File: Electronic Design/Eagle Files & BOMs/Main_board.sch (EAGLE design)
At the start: 35 parts, among them IC1 ACS712ELC-5A, IC2 ATMEGA328-PU, Q1 IRF9540, Q2 IRF9540, X1 16MHz

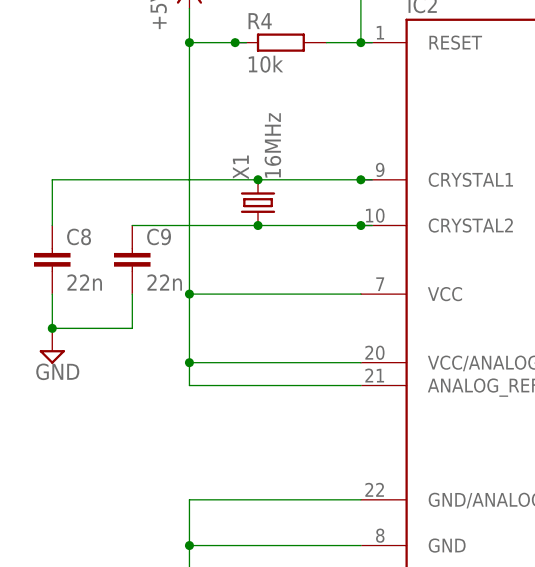
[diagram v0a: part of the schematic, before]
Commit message: correcting cap values on atmega crystal
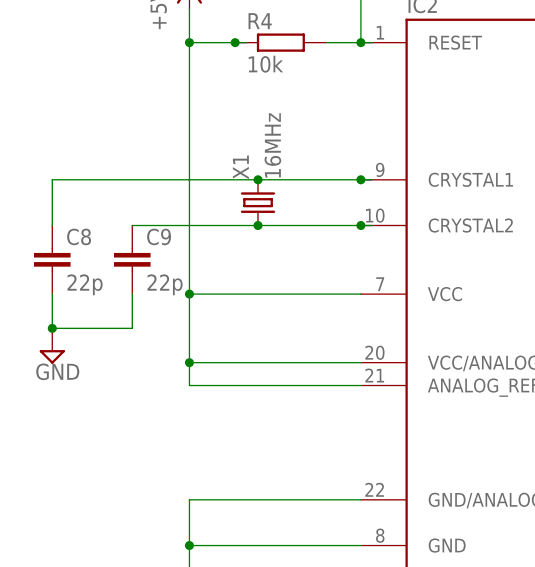
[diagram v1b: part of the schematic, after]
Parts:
- C8, C9: value 22n -> 22p
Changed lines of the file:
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@@
 <part name="+5V1" library="supply1" deviceset="+5V" device=""/>
 <part name="C7" library="resistor" deviceset="C-EU" device="C1206K" value="0.1u"/>
-<part name="C9" library="resistor" deviceset="C-EU" device="C0805K" value="22n"/>
-<part name="C8" library="resistor" deviceset="C-EU" device="C0805K" value="22n"/>
+<part name="C9" library="resistor" deviceset="C-EU" device="C0805K" value="22p"/>
+<part name="C8" library="resistor" deviceset="C-EU" device="C0805K" value="22p"/>
 <part name="SUPPLY14" library="supply2" deviceset="GND" device=""/>
 <part name="SUPPLY17" library="supply2" deviceset="GND" device=""/>

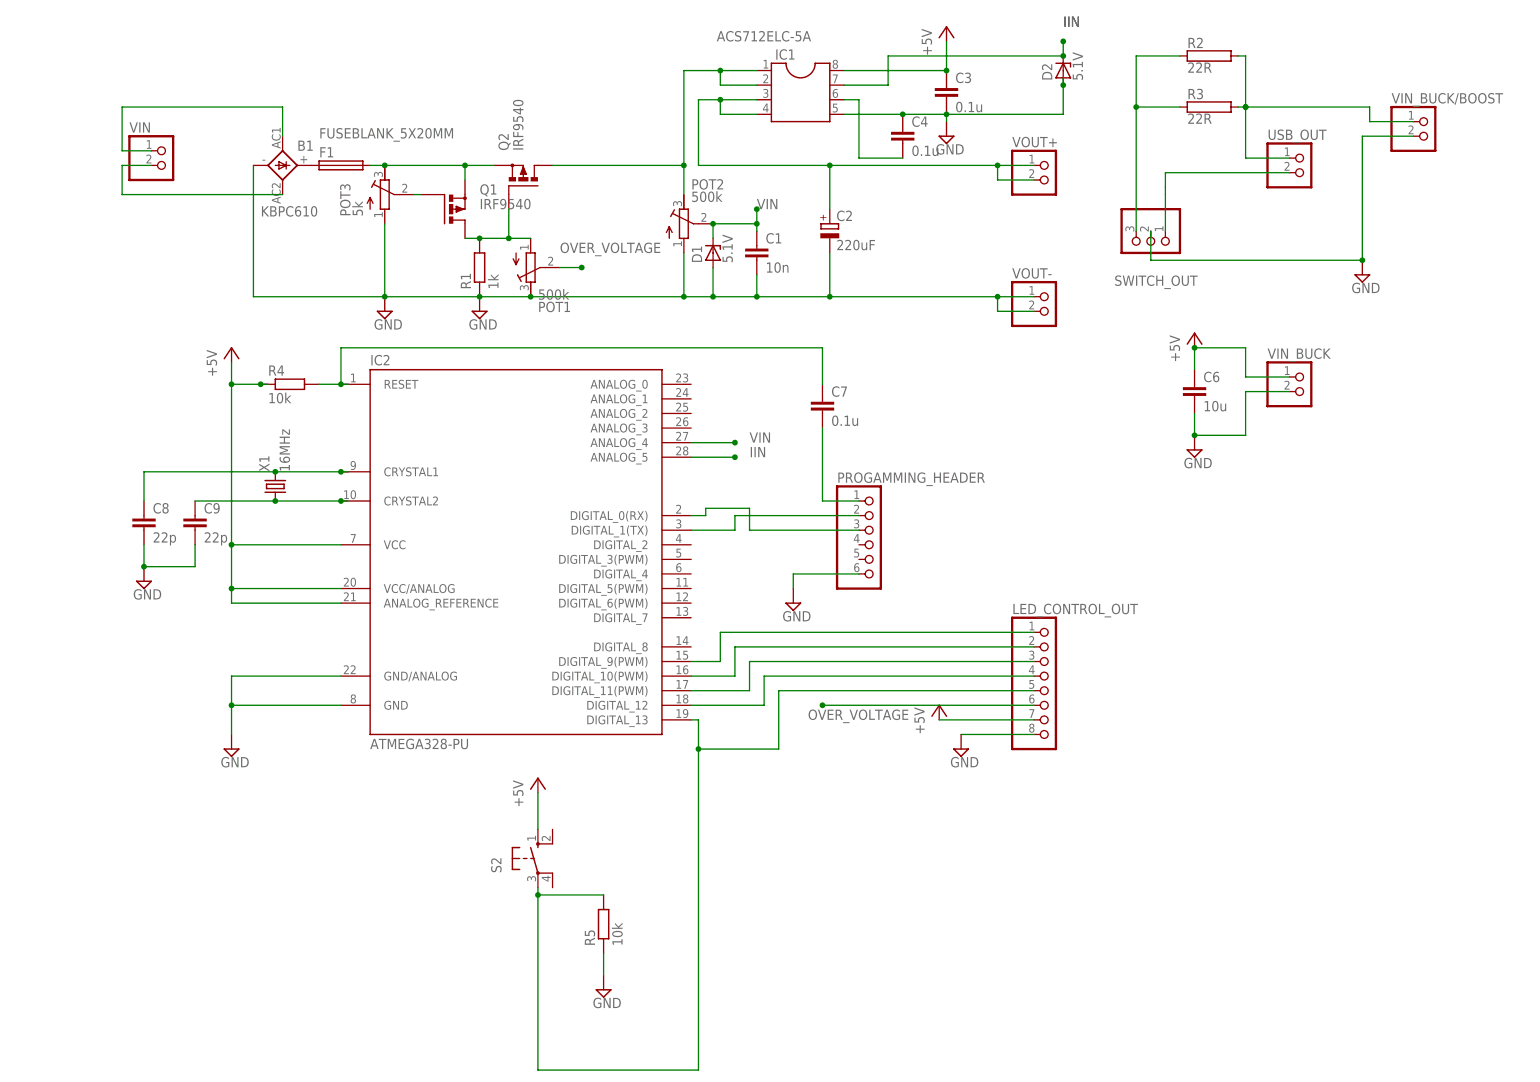
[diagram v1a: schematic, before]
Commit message: added overvoltage protection, replaced fuse holder footprint, stopped irfs from overlapping with ground stitching vias, moved dummy load resistors and corrected pin header pitch
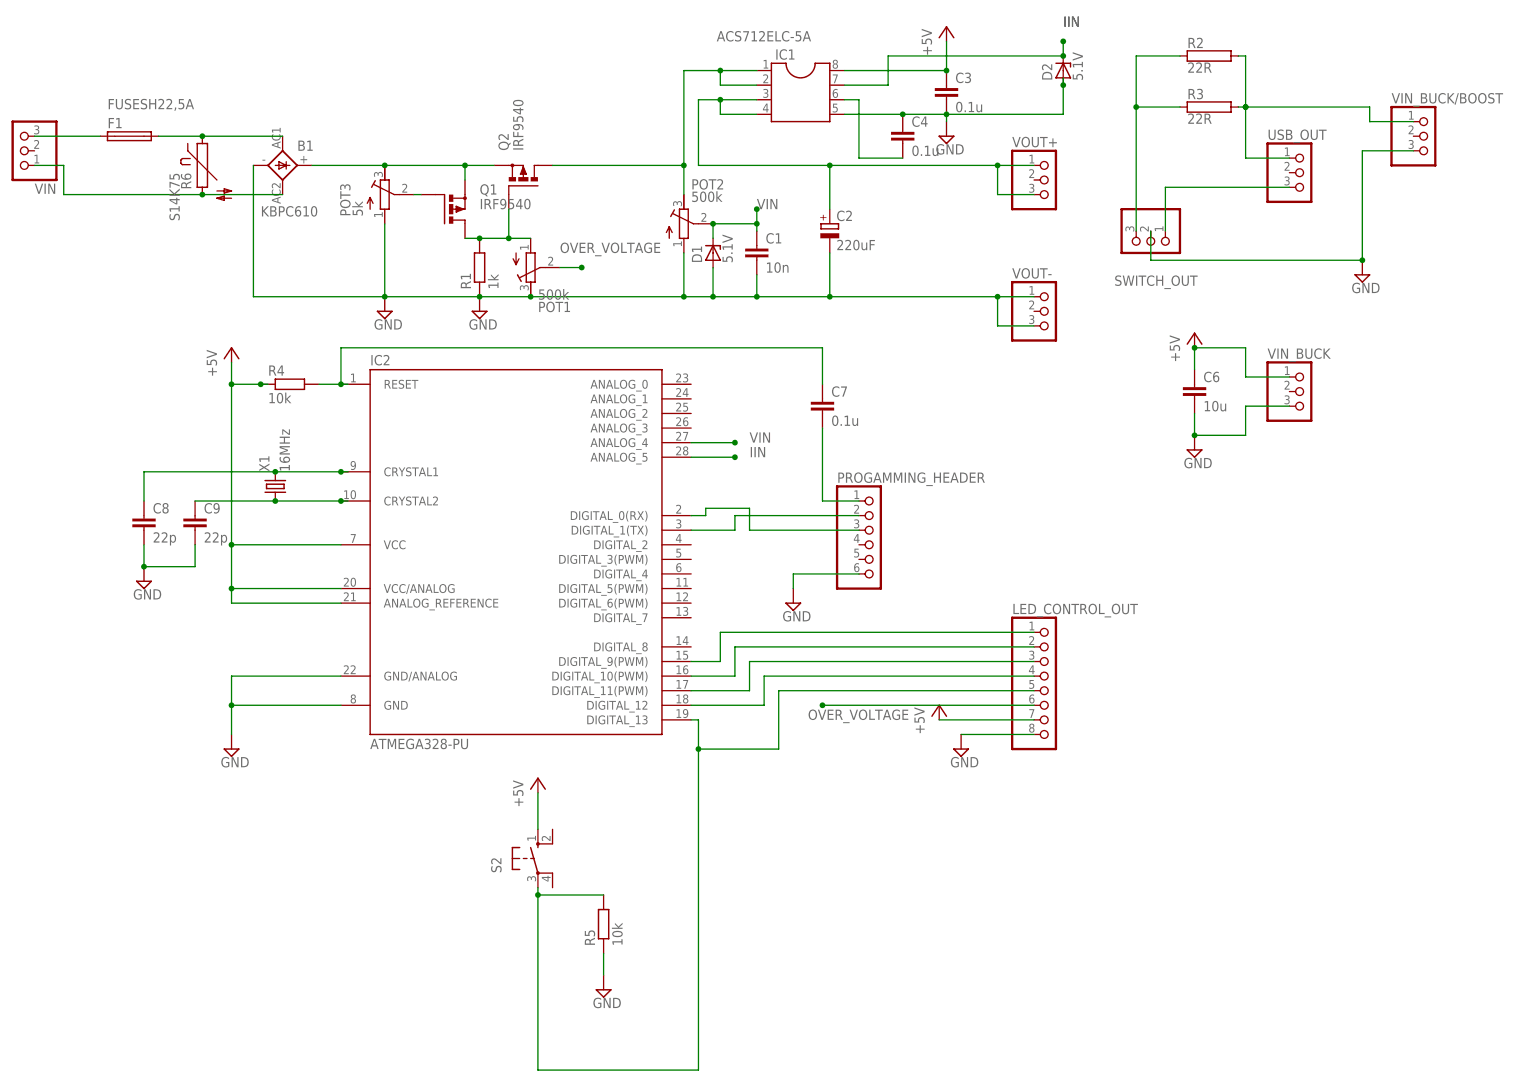
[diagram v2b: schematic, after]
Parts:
- added R6: S14K75, varistor:S14K17
- F1: value FUSEBLANK_5X20MM -> FUSESH22,5A; device fuse:FUSEBLANK_5X20MM -> fuse:FUSESH22,5A
- Q1, Q2: device transistor-power:PMOSFET_PTO220BV -> transistor-power:PMOSFET_PTO220BH
- USB_OUT, VIN, VIN_BUCK, VIN_BUCK/BOOST, VOUT+, VOUT-: device pinhead:PINHD-1X2 -> pinhead:PINHD-1X3
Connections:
- removed net N$20: B1.AC1, VIN.1
- removed net N$25: SWITCH_OUT.1, USB_OUT.2
- new net N$13: SWITCH_OUT.1, USB_OUT.3
- new net N$18: B1.AC1, F1.2, R6.1
- net GND: now also VIN_BUCK.3, VIN_BUCK/BOOST.3, VOUT-.3; no longer VIN_BUCK.2, VIN_BUCK/BOOST.2, VOUT-.2
- net M1S: now also VOUT+.3; no longer VOUT+.2
- net N$1: now also VIN.3; no longer B1.+
- net N$10: now also B1.+; no longer F1.2
- net N$19: now also R6.2, VIN.1; no longer VIN.2
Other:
- moved on the sheet: F1

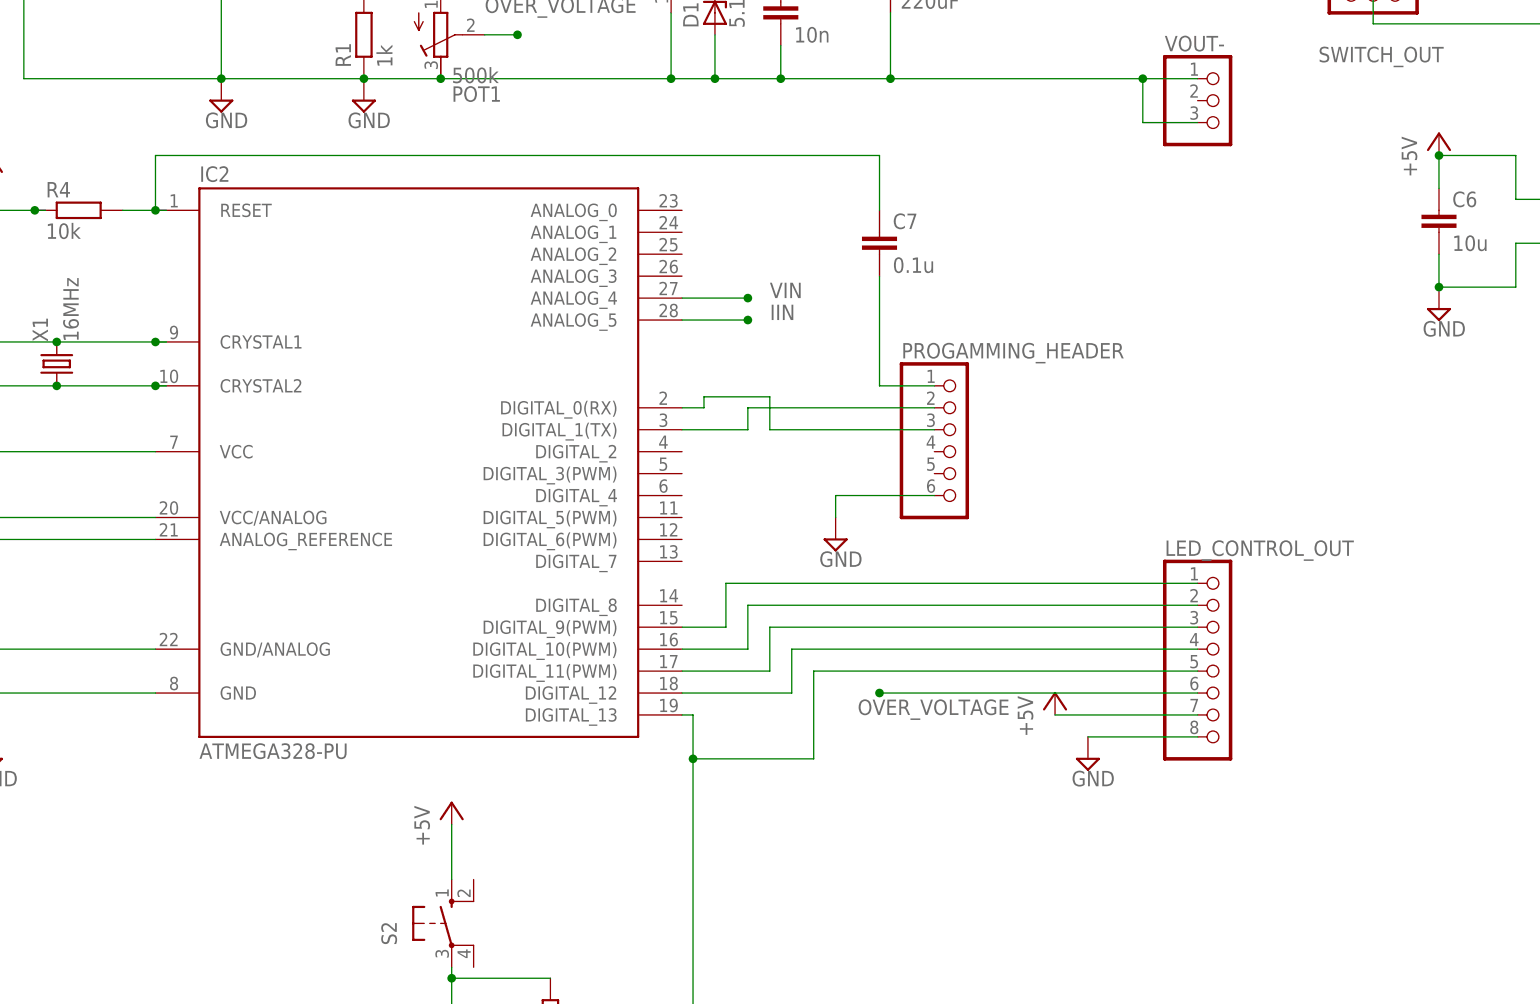
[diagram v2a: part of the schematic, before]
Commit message: adding breakout for atmega analog pins
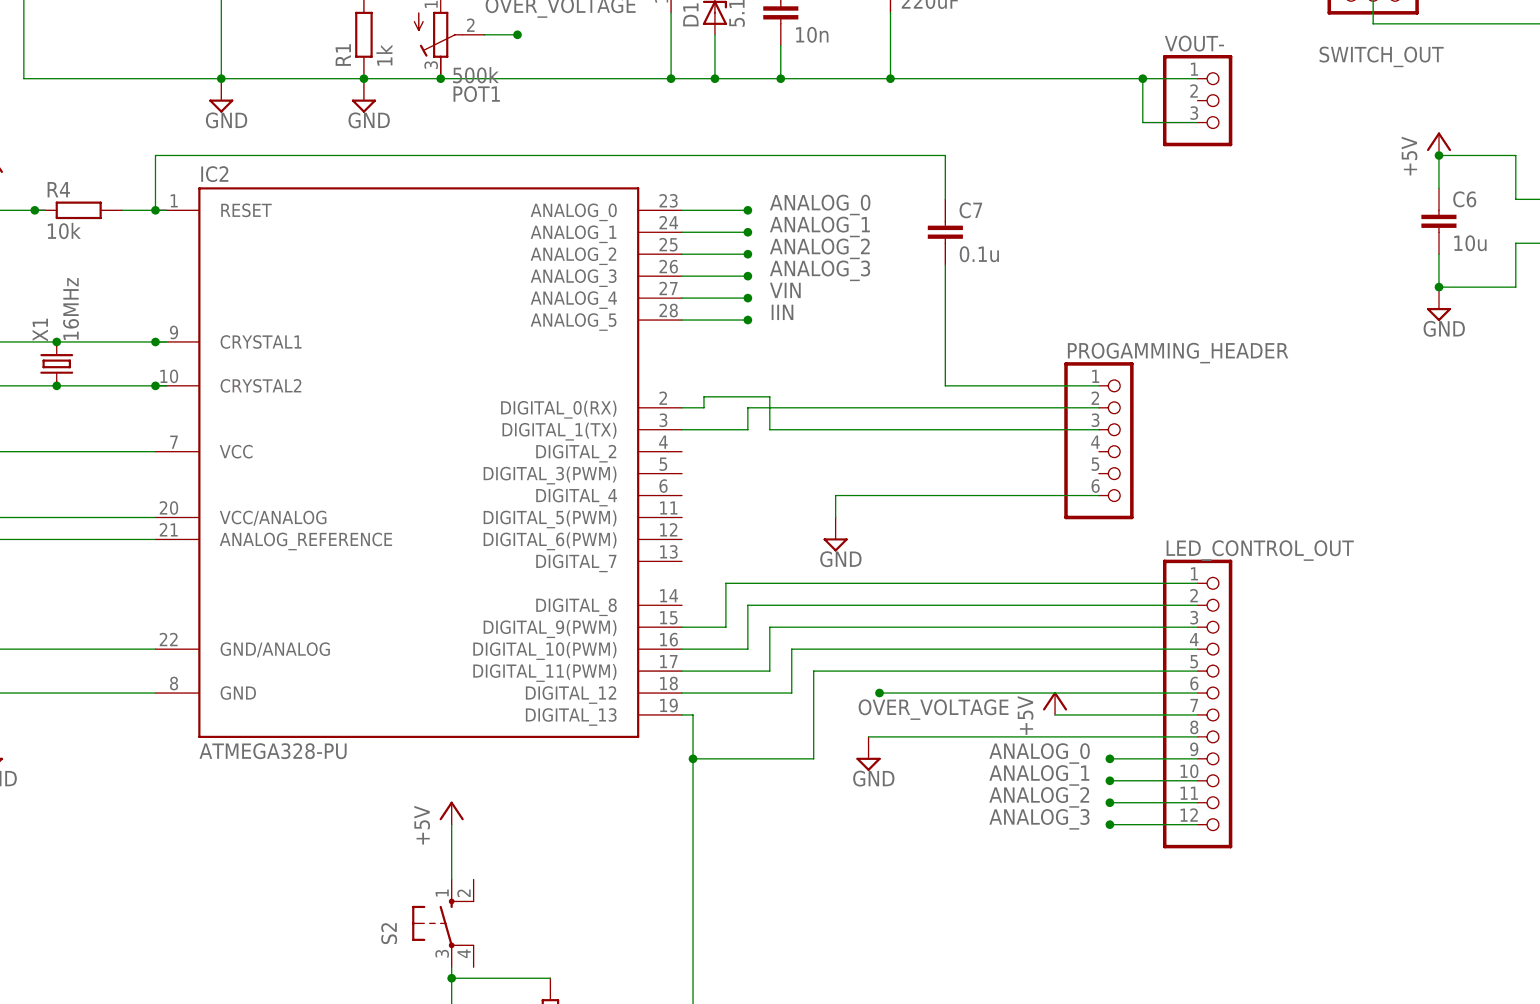
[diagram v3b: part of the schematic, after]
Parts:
- LED_CONTROL_OUT: device pinhead:PINHD-1X8 -> pinhead:PINHD-1X12
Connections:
- new net ANALOG_0: IC2.ANALOG_0, LED_CONTROL_OUT.9
- new net ANALOG_1: IC2.ANALOG_1, LED_CONTROL_OUT.10
- new net ANALOG_2: IC2.ANALOG_2, LED_CONTROL_OUT.11
- new net ANALOG_3: IC2.ANALOG_3, LED_CONTROL_OUT.12
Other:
- moved on the sheet: C7, PROGAMMING_HEADER
